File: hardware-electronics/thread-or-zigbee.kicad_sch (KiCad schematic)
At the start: 29 parts, among them J3 CONMHF1-SMD-T, U5 CP2102N-A02-GQFN20, U7 EFR32MG21B020F1024IM32-B, Y4 ABM8-38.400MHZ-10-D1G-T

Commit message: [#20] PCB DRC warnings WIP fix missing footprints
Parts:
- L1, L2, L3: footprint M2SmartHomeFootprints:L_0201_0603Metric -> M2SmartHomeFootprints:L_0201
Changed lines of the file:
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@@
 			)
 		)
-		(property "Footprint" "M2SmartHomeFootprints:L_0201_0603Metric"
+		(property "Footprint" "M2SmartHomeFootprints:L_0201"
 			(at 252.73 139.7 0)
 			(effects
@@
 			)
 		)
-		(property "Footprint" "M2SmartHomeFootprints:L_0201_0603Metric"
+		(property "Footprint" "M2SmartHomeFootprints:L_0201"
 			(at 134.62 109.22 0)
 			(effects
@@
 			)
 		)
-		(property "Footprint" "M2SmartHomeFootprints:L_0201_0603Metric"
+		(property "Footprint" "M2SmartHomeFootprints:L_0201"
 			(at 284.48 139.7 0)
 			(effects

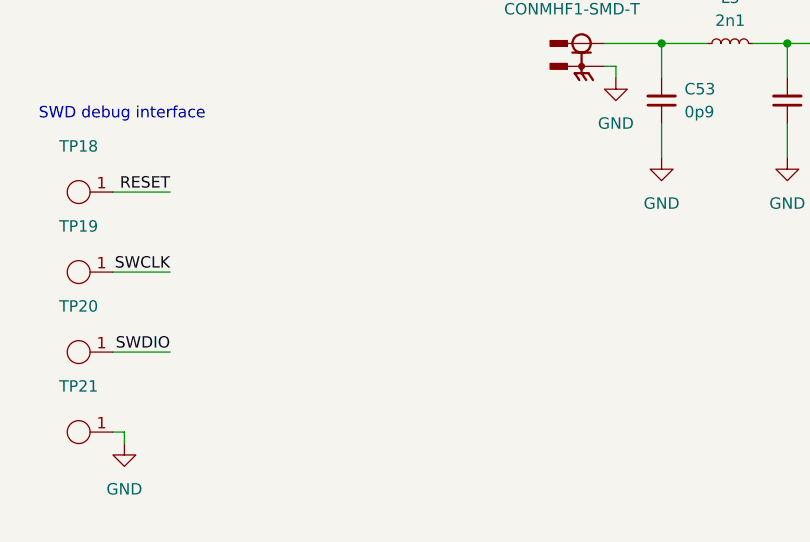
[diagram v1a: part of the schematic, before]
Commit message: [#24] PCB tag-connect programming connectors brainstorming
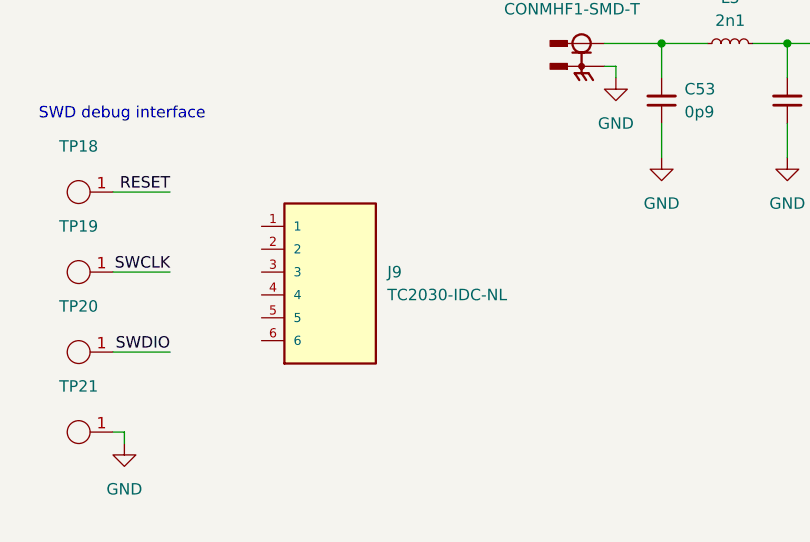
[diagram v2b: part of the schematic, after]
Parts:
- added J9: TC2030-IDC-NL, M2SmartHomeFootprints:TAG_TC2030-IDC-NL, symbol M2SmartHomeSymbols:TC2030-IDC-NL
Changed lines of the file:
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@@
+	)
+	(symbol
+		(lib_id "M2SmartHomeSymbols:TC2030-IDC-NL")
+		(at 72.39 124.46 0)
+		(unit 1)
+		(exclude_from_sim no)
+		(in_bom yes)
+		(on_board yes)
+		(dnp no)
+		(fields_autoplaced yes)
+		(property "Reference" "J9"
+			(at 78.74 121.9199 0)
+			(effects
+				(font
+					(size 1.27 1.27)
+				)
+				(justify left)
+			)
+		)
+		(property "Value" "TC2030-IDC-NL"
+			(at 78.74 124.4599 0)
+			(effects
+				(font
+					(size 1.27 1.27)
+				)
+				(justify left)
+			)
+		)
+		(property "Footprint" "M2SmartHomeFootprints:TAG_TC2030-IDC-NL"
+			(at 72.39 124.46 0)
+			(effects
+				(font
+					(size 1.27 1.27)
+				)
+				(justify bottom)
+				(hide yes)
+			)
+		)
+		(property "Datasheet" ""
+			(at 72.39 124.46 0)
+			(effects
+				(font
+					(size 1.27 1.27)
+				)
+				(hide yes)
+			)
+		)
+		(property "Description" ""
+			(at 72.39 124.46 0)
+			(effects
+				(font
+					(size 1.27 1.27)
+				)
+				(hide yes)
+			)
+		)
+		(property "MF" "Tag-Connect"
+			(at 72.39 124.46 0)
+			(effects
+				(font
+					(size 1.27 1.27)
+				)
+				(justify bottom)
+				(hide yes)
+			)
+		)
+		(property "Description_1" "\n                        \n                            PLUG-OF-NAILS 6-PIN W/O LEGS 8\n                        \n"
+			(at 72.39 124.46 0)
+			(effects
+				(font
+					(size 1.27 1.27)
+				)
+				(justify bottom)
+				(hide yes)
+			)
+		)
+		(property "Package" "None"
+			(at 72.39 124.46 0)
+			(effects
+				(font
+					(size 1.27 1.27)
+				)
+				(justify bottom)
+				(hide yes)
+			)
+		)
+		(property "Price" "None"
+			(at 72.39 124.46 0)
+			(effects
+				(font
+					(size 1.27 1.27)
+				)
+				(justify bottom)
+				(hide yes)
+			)
+		)
+		(property "Check_prices" "https://www.snapeda.com/parts/TC2030-IDC-NL/Tag-Connect/view-part/?ref=eda"
+			(at 72.39 124.46 0)
+			(effects
+				(font
+					(size 1.27 1.27)
+				)
+				(justify bottom)
+				(hide yes)
+			)
+		)
+		(property "STANDARD" "Manufacturer recommendation"
+			(at 72.39 124.46 0)
+			(effects
+				(font
+					(size 1.27 1.27)
+				)
+				(justify bottom)
+				(hide yes)
+			)
+		)
+		(property "PARTREV" "MS"
+			(at 72.39 124.46 0)
+			(effects
+				(font
+					(size 1.27 1.27)
+				)
+				(justify bottom)
+				(hide yes)
+			)
+		)
+		(property "SnapEDA_Link" "https://www.snapeda.com/parts/TC2030-IDC-NL/Tag-Connect/view-part/?ref=snap"
+			(at 72.39 124.46 0)
+			(effects
+				(font
+					(size 1.27 1.27)
+				)
+				(justify bottom)
+				(hide yes)
+			)
+		)
+		(property "MP" "TC2030-IDC-NL"
+			(at 72.39 124.46 0)
+			(effects
+				(font
+					(size 1.27 1.27)
+				)
+				(justify bottom)
+				(hide yes)
+			)
+		)
+		(property "Availability" "Not in stock"
+			(at 72.39 124.46 0)
+			(effects
+				(font
+					(size 1.27 1.27)
+				)
+				(justify bottom)
+				(hide yes)
+			)
+		)
+		(property "MANUFACTURER" "Tag-Connect"
+			(at 72.39 124.46 0)
+			(effects
+				(font
+					(size 1.27 1.27)
+				)
+				(justify bottom)
+				(hide yes)
+			)
+		)
+		(pin "6"
+		)
+		(pin "2"
+		)
+		(pin "5"
+		)
+		(pin "4"
+		)
+		(pin "3"
+		)
+		(pin "1"
+		)
+		(instances
+			(project "M2SmartHome"
+				(path "/da663dec-9e91-4003-a791-431d460ad63c/a351a459-aa5d-43cb-82d3-d5bdf9396bea"
+					(reference "J9")
+					(unit 1)
+				)
+			)
+		)
 	)
 	(symbol

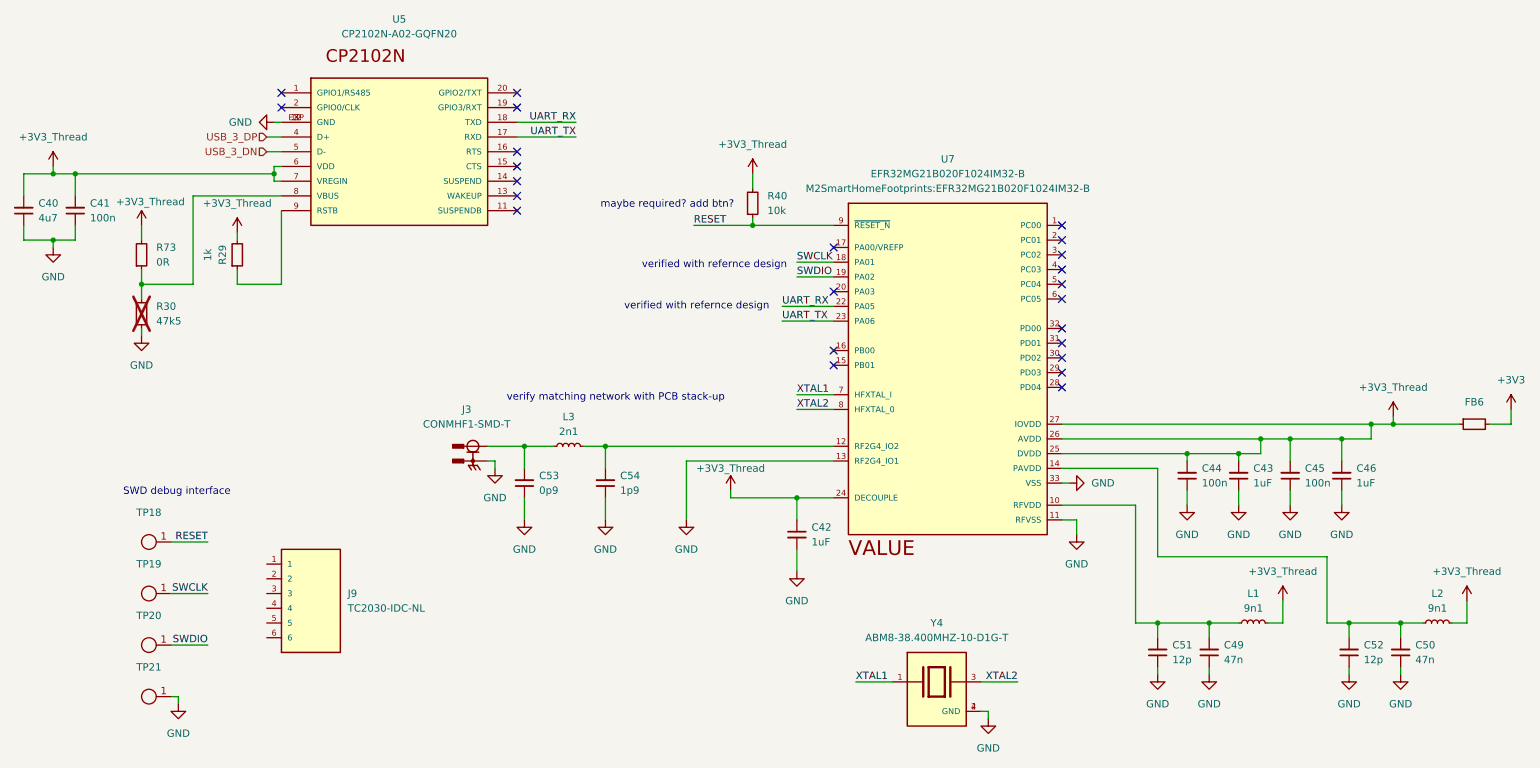
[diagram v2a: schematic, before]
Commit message: [#26] Remove power plane splits for invidual devices
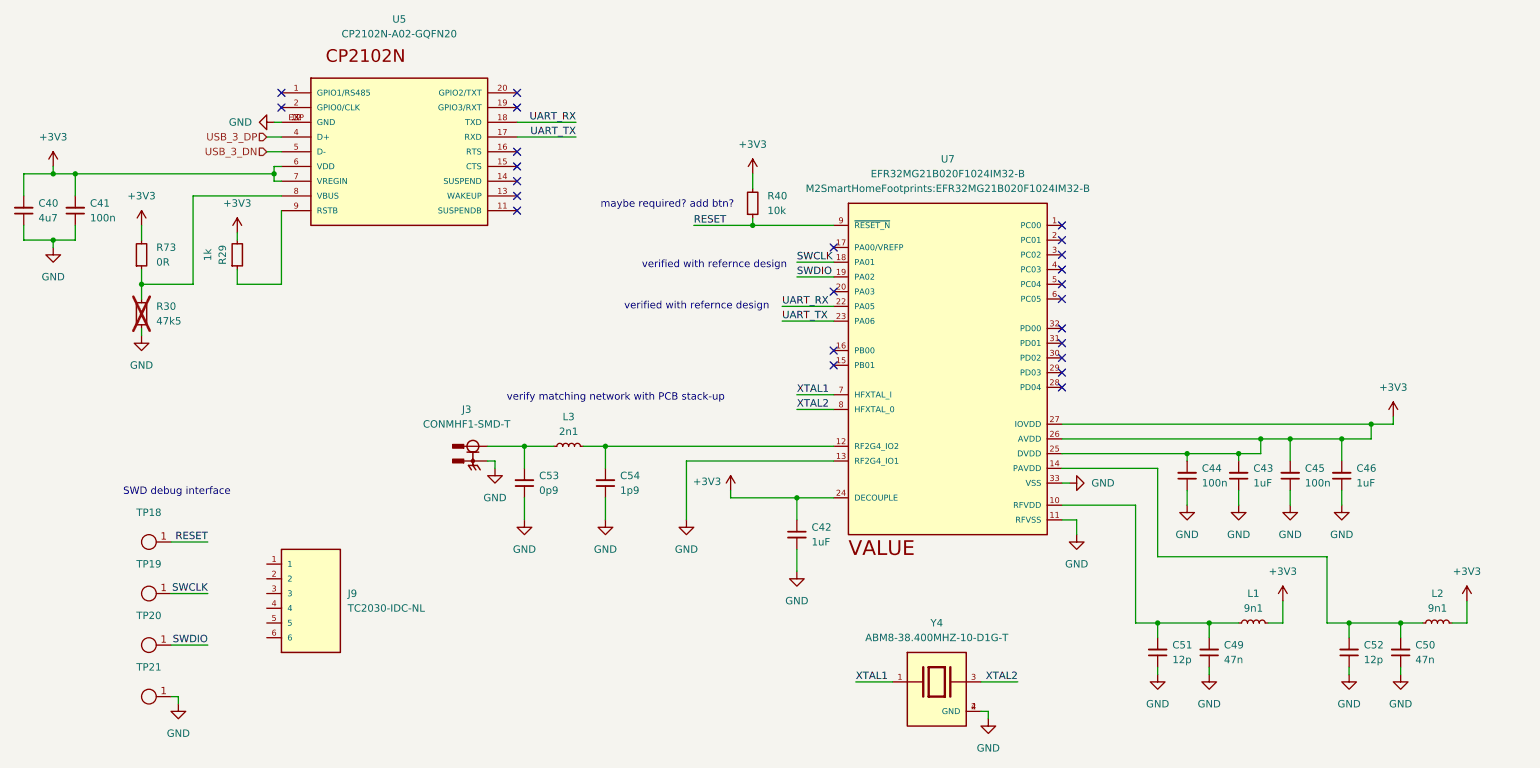
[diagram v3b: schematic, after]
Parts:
- removed FB6: FB_120R_0603, M2SmartHomeFootprints:FB_0603, symbol M2SmartHomeSymbols:FB_120R_0603
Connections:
- net +3V3_Thread is gone; now on net +3V3: C40.2, C41.2, C42.1, C43.2, C44.2, C45.2, C46.2, L1.2, L2.2, R29.2, R40.2, R73.2, U5.6 (VDD), U5.7 (VREGIN), U7.24 (DECOUPLE), U7.25 (DVDD), U7.26 (AVDD), U7.27 (IOVDD)

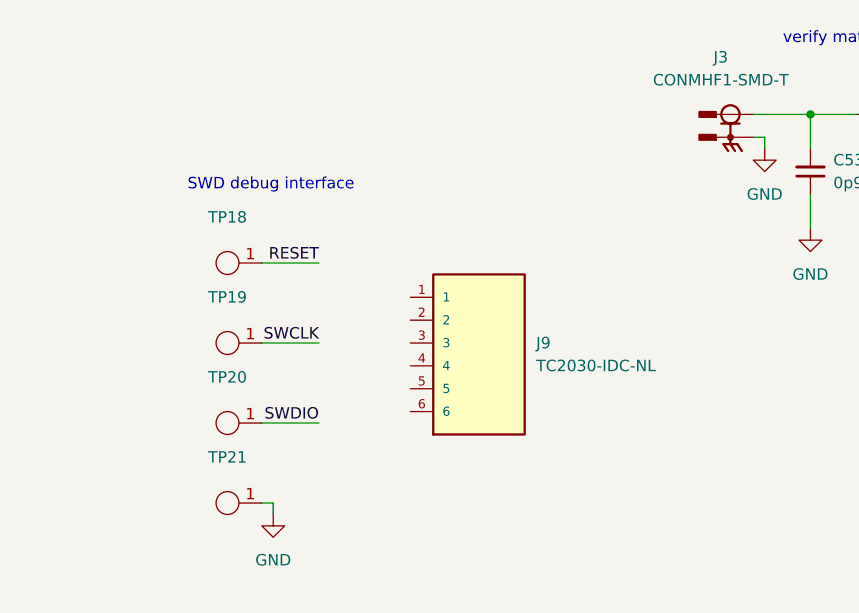
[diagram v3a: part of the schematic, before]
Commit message: [#26] Add programing interface for silicon labs MCU
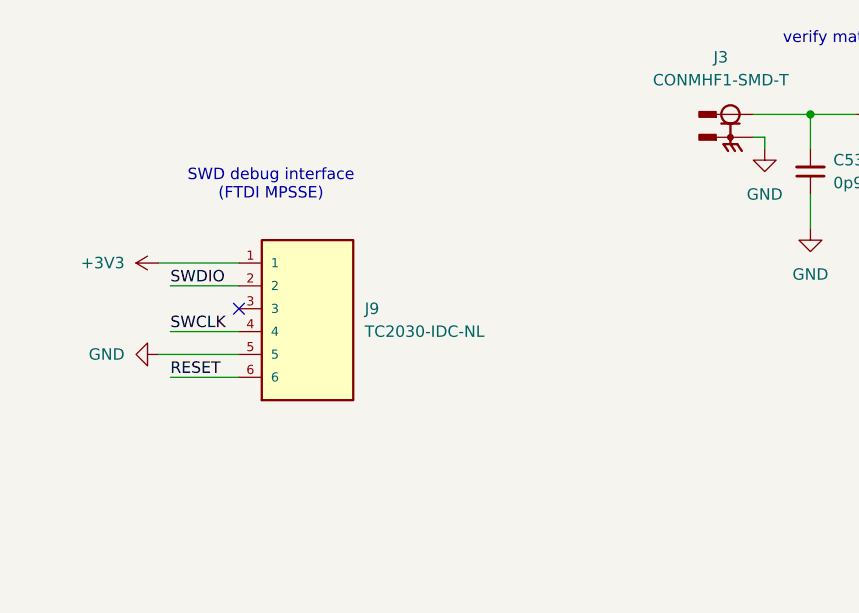
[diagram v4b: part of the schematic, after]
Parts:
- removed TP18, TP19, TP20, TP21: ~, M2SmartHomeFootprints:TestPoint_Pad_D1.0mm, symbol M2SmartHomeSymbols:TP_SMD_1mm
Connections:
- net +3V3: now also J9.1
- net GND: now also J9.5
- net RESET: now also J9.6
- net SWCLK: now also J9.4
- net SWDIO: now also J9.2
- no-connect marks 24 -> 25
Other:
- note added: "SWD debug interface (FTDI MPSSE)"
- note removed: "SWD debug interface"
- moved on the sheet: J9

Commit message: [#27] Add BOM for rev 1.1.0
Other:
- note removed: "maybe required? add btn?"
- note removed: "verified with refernce design"
- note removed: "verify matching network with PCB stack-up"
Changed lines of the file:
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@@
-		)
-	)
-	(text "verified with refernce design"
-		(exclude_from_sim no)
-		(at 141.986 65.278 0)
-		(effects
-			(font
-				(size 1.27 1.27)
-			)
-		)
-	)
-	(text "verify matching network with PCB stack-up"
-		(exclude_from_sim no)
-		(at 124.968 88.138 0)
-		(effects
-			(font
-				(size 1.27 1.27)
-			)
-		)
-	)
-	(text "maybe required? add btn?"
-		(exclude_from_sim no)
-		(at 133.858 54.864 0)
-		(effects
-			(font
-				(size 1.27 1.27)
-			)
 		)
 	)
@@
 		(effects
 			(font
-				(size 1.27 1.27)
-			)
-		)
-	)
-	(text "verified with refernce design"
-		(exclude_from_sim no)
-		(at 138.938 72.39 0)
-		(effects
-			(font

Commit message: [#26] Correct MPN GRM155R61A104KA01D
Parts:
- C41, C44, C45: Author Your Name -> Lukasz Nowarkiewicz; MPN GRM155R61A104KE01D -> GRM155R61A104KA01D
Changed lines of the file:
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@@
 			)
 		)
-		(property "MPN" "GRM155R61A104KE01D"
+		(property "MPN" "GRM155R61A104KA01D"
 			(at 49.53 38.1 0)
 			(effects
@@
 			)
 		)
-		(property "Author" "Your Name"
+		(property "Author" "Lukasz Nowarkiewicz"
 			(at 57.15 38.1 0)
 			(effects
@@
 			)
 		)
-		(property "MPN" "GRM155R61A104KE01D"
+		(property "MPN" "GRM155R61A104KA01D"
 			(at 241.3 83.82 0)
 			(effects
@@
 			)
 		)
-		(property "Author" "Your Name"
+		(property "Author" "Lukasz Nowarkiewicz"
 			(at 248.92 83.82 0)
 			(effects
@@
 			)
 		)
-		(property "MPN" "GRM155R61A104KE01D"
+		(property "MPN" "GRM155R61A104KA01D"
 			(at 259.08 83.82 0)
 			(effects
@@
 			)
 		)
-		(property "Author" "Your Name"
+		(property "Author" "Lukasz Nowarkiewicz"
 			(at 266.7 83.82 0)
 			(effects

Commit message: [#26] Correct MPN GRM155R61H105KE05D
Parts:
- C42, C43, C46: Author Your Name -> Lukasz Nowarkiewicz; MPN GRM155R61H105KE92D -> GRM155R61H105KE05D
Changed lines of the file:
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@@
 			)
 		)
-		(property "MPN" "GRM155R61H105KE92D"
+		(property "MPN" "GRM155R61H105KE05D"
 			(at 267.97 83.82 0)
 			(effects
@@
 			)
 		)
-		(property "Author" "Your Name"
+		(property "Author" "Lukasz Nowarkiewicz"
 			(at 275.59 83.82 0)
 			(effects
@@
 			)
 		)
-		(property "MPN" "GRM155R61H105KE92D"
+		(property "MPN" "GRM155R61H105KE05D"
 			(at 250.19 83.82 0)
 			(effects
@@
 			)
 		)
-		(property "Author" "Your Name"
+		(property "Author" "Lukasz Nowarkiewicz"
 			(at 257.81 83.82 0)
 			(effects
@@
 			)
 		)
-		(property "MPN" "GRM155R61H105KE92D"
+		(property "MPN" "GRM155R61H105KE05D"
 			(at 138.43 129.54 0)
 			(effects
@@
 			)
 		)
-		(property "Author" "Your Name"
+		(property "Author" "Lukasz Nowarkiewicz"
 			(at 130.81 129.54 0)
 			(effects

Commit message: [#26] Correct MPN GRM1555C1H120GA01D
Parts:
- C51, C52: Author Your Name -> Lukasz Nowarkiewicz; MPN GRM155R71H120KA01D -> GRM1555C1H120GA01D
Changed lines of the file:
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@@
 			)
 		)
-		(property "Description" "SMD Multilayer Ceramic Capacitor, 12 pF, 50 V, 0402 [1005 Metric], ±10%, X7R, GRM Series"
+		(property "Description" "SMD Multilayer Ceramic Capacitor, 12 pF, 50 V, 0402 [1005 Metric], ±2%, C0G, GRM Series"
 			(at 218.44 134.62 0)
 			(effects
@@
 			)
 		)
-		(property "MPN" "GRM155R71H120KA01D"
+		(property "MPN" "GRM1555C1H120GA01D"
 			(at 236.22 114.3 0)
 			(effects
@@
 			)
 		)
-		(property "Author" "Your Name"
+		(property "Author" "Lukasz Nowarkiewicz"
 			(at 243.84 114.3 0)
 			(effects
@@
 			)
 		)
-		(property "Description" "SMD Multilayer Ceramic Capacitor, 12 pF, 50 V, 0402 [1005 Metric], ±10%, X7R, GRM Series"
+		(property "Description" "SMD Multilayer Ceramic Capacitor, 12 pF, 50 V, 0402 [1005 Metric], ±2%, C0G, GRM Series"
 			(at 251.46 134.62 0)
 			(effects
@@
 			)
 		)
-		(property "MPN" "GRM155R71H120KA01D"
+		(property "MPN" "GRM1555C1H120GA01D"
 			(at 269.24 114.3 0)
 			(effects
@@
 			)
 		)
-		(property "Author" "Your Name"
+		(property "Author" "Lukasz Nowarkiewicz"
 			(at 276.86 114.3 0)
 			(effects
